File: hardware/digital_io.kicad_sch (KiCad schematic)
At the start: 0 parts

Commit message: block refactoring
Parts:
- added C7, C8, C9: 1uF, Capacitor_SMD:C_0603_1608Metric, symbol Device:C
- added D12, D8: D_TVS_30V, Diode_SMD:D_SMB, symbol Device:D_TVS
- added J5: Conn_01x02/DIN, TerminalBlock:TerminalBlock_Altech_AK300-2_P5.00mm, symbol Connector_Generic:Conn_01x02
- added JP3: SolderJumper_3_Bridged12, Jumper:SolderJumper-3_P1.3mm_Bridged12_Pad1.0x1.5mm_NumberLabels, symbol Jumper:SolderJumper_3_Bridged12
- added R10, R9: 100k, Resistor_SMD:R_0603_1608Metric, symbol Device:R
- added R11, R19: 1M, Resistor_SMD:R_0603_1608Metric, symbol Device:R
- added R12, R14: 5.1K, Resistor_SMD:R_0603_1608Metric, symbol Device:R
- added U3: LM393, Package_SO:SOP-8_3.9x4.9mm_P1.27mm, symbol Comparator:LM393
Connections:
- new net: D8.1 (A1), R19.1, R9.1, U3.3 (+)
- new net: D12.1 (A1), R10.1, R11.1, U3.5 (+)
- new net +3.3V: C7.1, JP3.1 (A), R12.1, R14.1, U3.8 (V+)
- new net +5V: JP3.3 (B)
- new net DIN1: C8.1, R14.2, R19.2, U3.1
- new net DIN2: C9.1, R11.2, R12.2, U3.7
- new net DIN_LINE1: J5.1 (Pin_1), R9.2
- new net DIN_LINE2: J5.2 (Pin_2), R10.2
- new net DIN_VREF: JP3.2 (C), U3.2 (-), U3.6 (-)
- new net GND: C7.2, C8.2, C9.2, D12.2 (A2), D8.2 (A2), U3.4 (V-)
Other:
- note added: "Digital Input 0-VIN 100mV Hysteresis"
- note added: "TODO: Decide whether it's worth having digitally adjustable Vref"

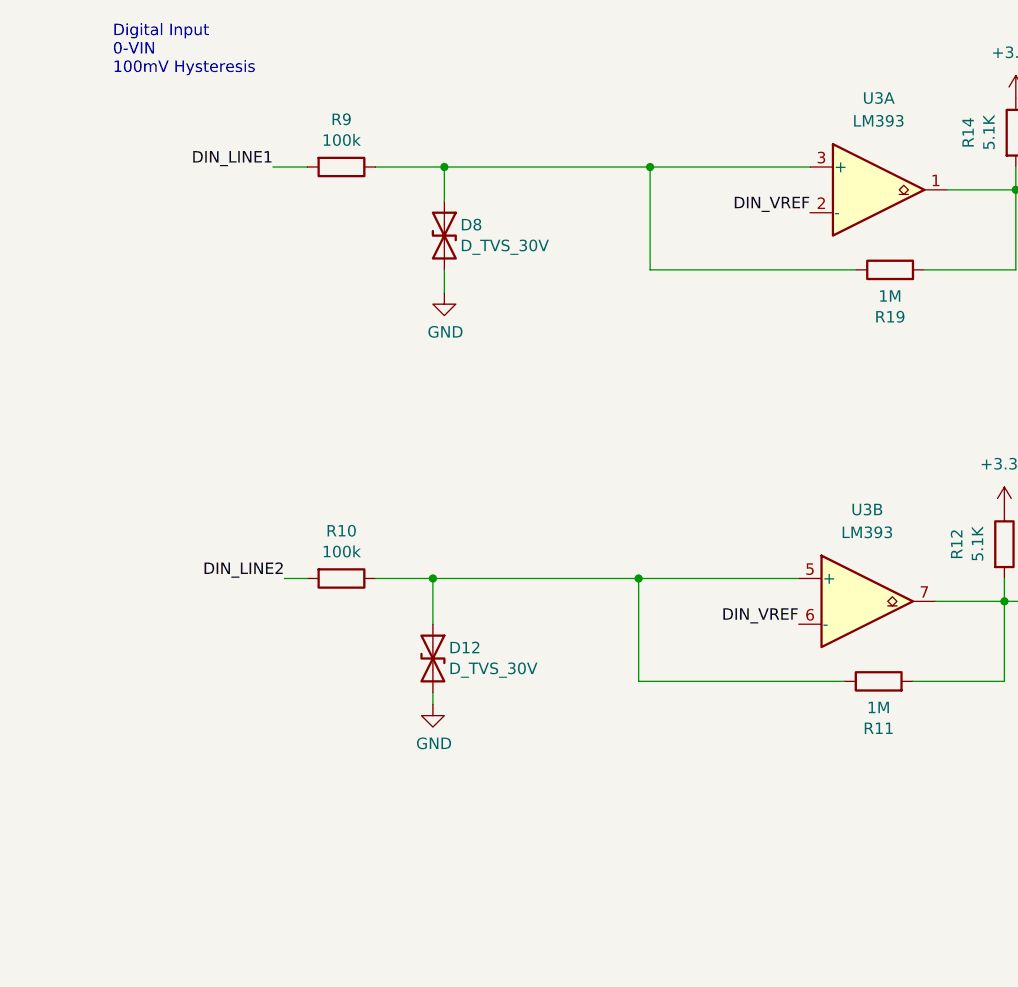
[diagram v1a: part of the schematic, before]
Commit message: moving subsheets to blocks
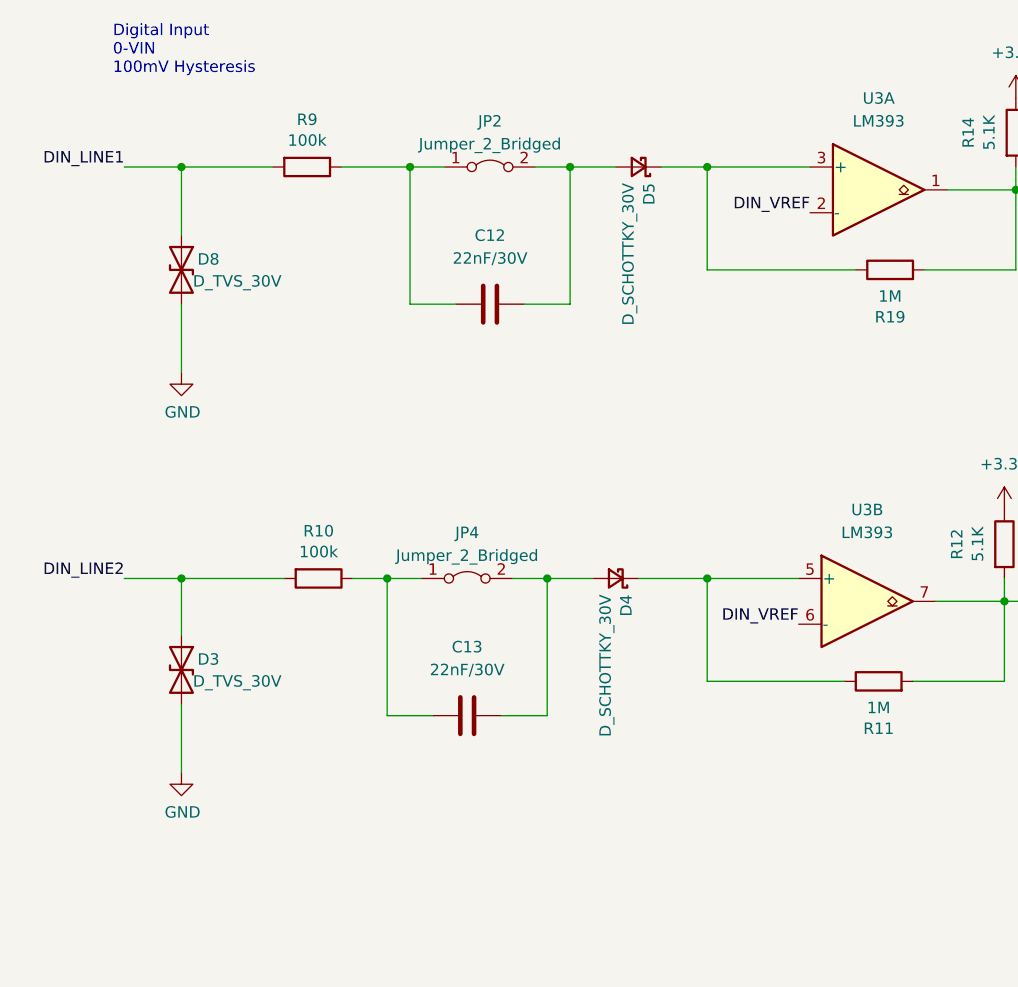
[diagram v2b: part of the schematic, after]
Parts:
- removed D12: D_TVS_30V, Diode_SMD:D_SMB, symbol Device:D_TVS
- added C12, C13: 22nF/30V, Capacitor_SMD:C_0603_1608Metric, symbol Device:C
- added D3: D_TVS_30V, Diode_SMD:D_SMB, symbol Device:D_TVS
- added D4, D5: D_SCHOTTKY_30V, Diode_SMD:D_SOD-123, symbol Device:D_Schottky_Small
- added JP2, JP4: Jumper_2_Bridged, Connector_PinHeader_1.00mm:PinHeader_1x02_P1.00mm_Vertical, symbol Jumper:Jumper_2_Bridged
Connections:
- net DIN_LINE1: now also D8.1 (A1)
- net DIN_LINE2: now also D3.1 (A1)
- net GND: now also D3.2 (A2)
- net at R19.1, U3.3 (+): now also D5.1 (K); no longer D8.1 (A1), R9.1
- net at R11.1, U3.5 (+): now also D4.1 (K); no longer R10.1
- new net: C13.2, JP4.1 (A), R10.1
- new net: C13.1, D4.2 (A), JP4.2 (B)
- new net: C12.2, JP2.1 (A), R9.1
- new net: C12.1, D5.2 (A), JP2.2 (B)
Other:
- moved on the sheet: D8, R10, R9
